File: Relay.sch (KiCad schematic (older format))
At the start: 0 parts

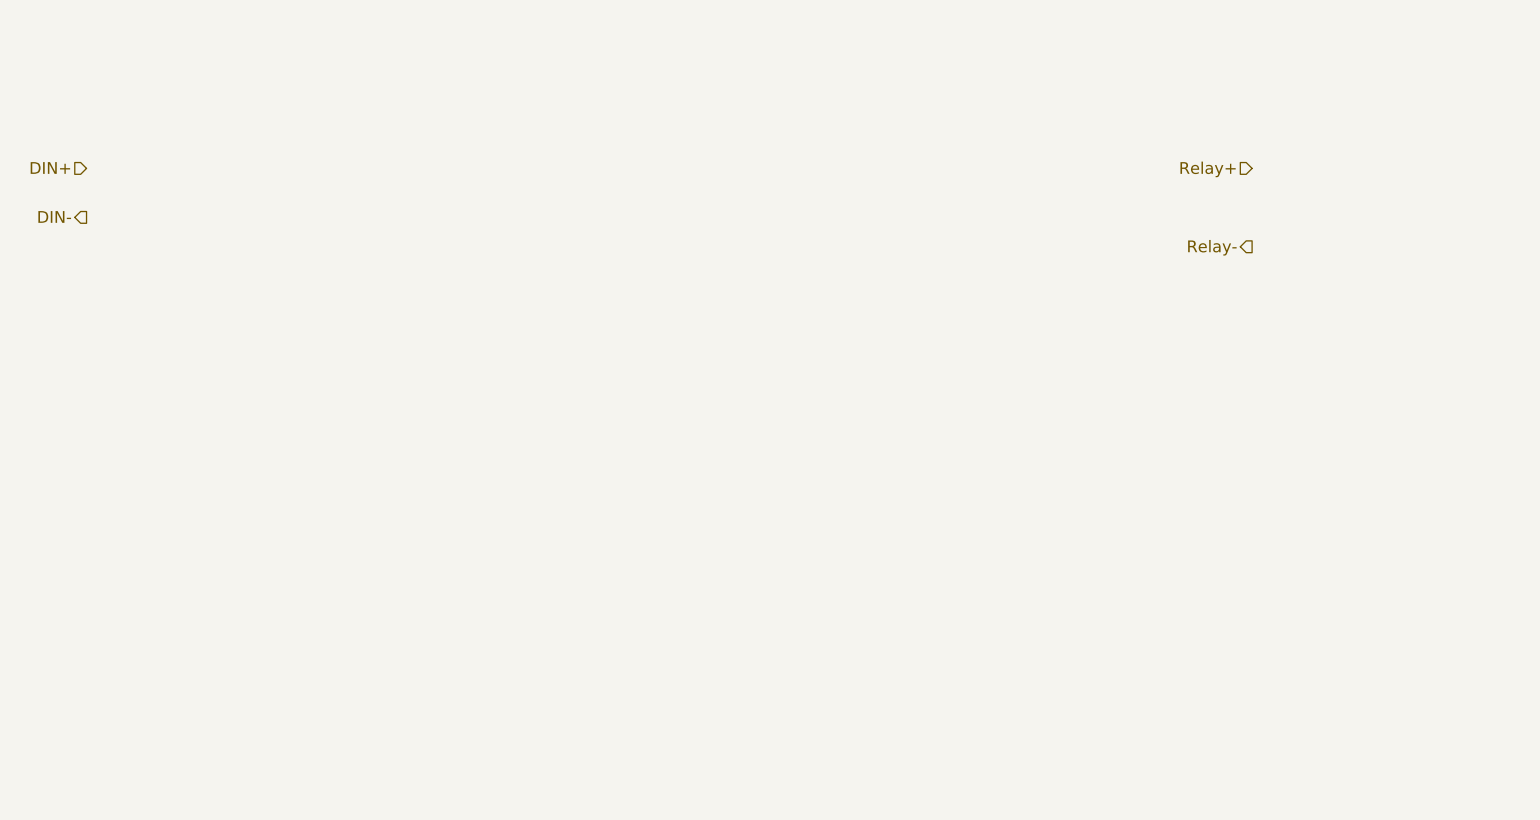
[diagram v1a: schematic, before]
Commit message: Added Relay module outline
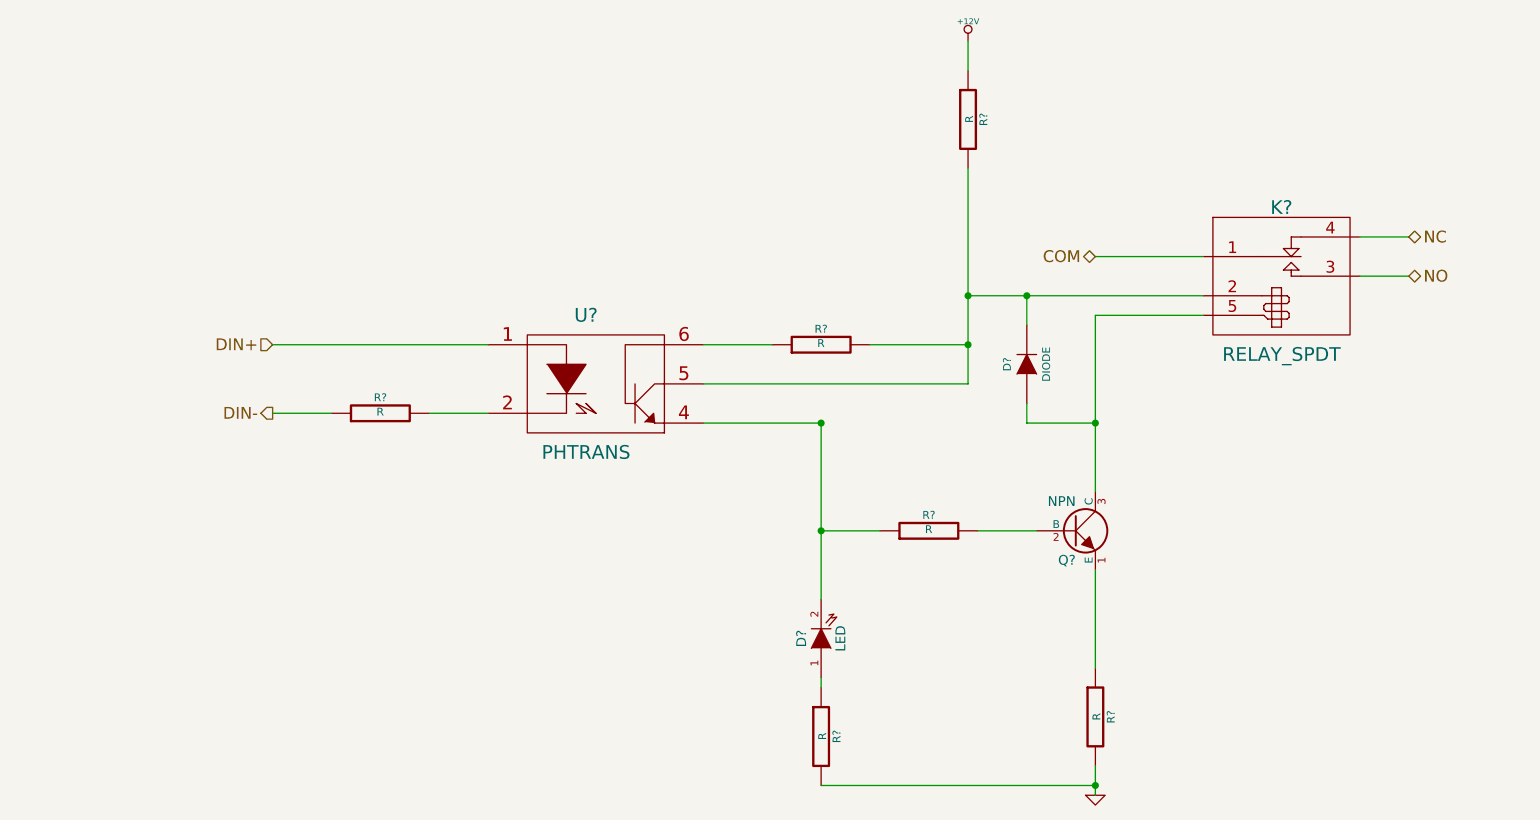
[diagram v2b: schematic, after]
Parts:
- added D?: LED, ~, symbol LED
- added D?: DIODE, ~, symbol DIODE
- added K?: RELAY_SPDT, ~, symbol RELAY_SPDT
- added Q?: NPN, ~, symbol NPN
- added R? (x6): R, ~, symbol R
- added U?: PHTRANS, ~, symbol PHTRANS
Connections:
- net DIN+: now also U?.1
- net DIN-: now also R?.1
- new net: R?.2, U?.2
- new net: D?.2 (K), R?.1, U?.4
- new net: D?.2 (K), K?.2 (Coil+), R?.2, R?.2, U?.5
- new net: R?.1, U?.6
- new net: Q?.2 (B), R?.2
- new net: Q?.1 (E), R?.1
- new net: D?.1 (A), K?.5 (Coil-), Q?.3 (C)
- new net: D?.1 (A), R?.1
- new net +12V: R?.1
- new net COM: K?.1 (C1)
- new net GND: R?.2, R?.2
- new net NC: K?.4 (R1)
- new net NO: K?.3 (T1)
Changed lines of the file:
@@
 LIBS:contrib
 LIBS:valves
+LIBS:BenchBudEE
 LIBS:BenchBudEE-cache
 EELAYER 27 0
@@
 Comment4 ""
 $EndDescr
-Text HLabel 2450 2500 0    60   Input ~ 0
+Text HLabel 3400 3400 0    60   Input ~ 0
 DIN+
-Text HLabel 2450 2750 0    60   Output ~ 0
+Text HLabel 3400 3750 0    60   Output ~ 0
 DIN-
-Text HLabel 8400 2500 0    60   Input ~ 0
-Relay+
-Text HLabel 8400 2900 0    60   Output ~ 0
-Relay-
+Text HLabel 9200 3050 2    60   BiDi ~ 0
+NO
+Text HLabel 9200 2850 2    60   BiDi ~ 0
+NC
+$Comp
+L PHTRANS U?
+U 1 1 52EFBD6E
+P 5050 3600
+F 0 "U?" H 5000 3950 70  0000 C CNN
+F 1 "PHTRANS" H 5000 3250 70  0000 C CNN
+F 2 "~" H 5050 3600 60  0000 C CNN
+F 3 "~" H 5050 3600 60  0000 C CNN
+	1    5050 3600
+	1    0    0    -1
+$EndComp
+$Comp
+L R R?
+U 1 1 52EFBD7D
+P 6750 4350
+F 0 "R?" V 6830 4350 40  0000 C CNN
+F 1 "R" V 6757 4351 40  0000 C CNN
+F 2 "~" V 6680 4350 30  0000 C CNN
+F 3 "~" H 6750 4350 30  0000 C CNN
+	1    6750 4350
+	0    -1   -1   0
+$EndComp
+$Comp
+L NPN Q?
+U 1 1 52EFBDE3
+P 7500 4350
+F 0 "Q?" H 7500 4200 50  0000 R CNN
+F 1 "NPN" H 7500 4500 50  0000 R CNN
+F 2 "~" H 7500 4350 60  0000 C CNN
+F 3 "~" H 7500 4350 60  0000 C CNN
+	1    7500 4350
+	1    0    0    -1
+$EndComp
+$Comp
+L LED D?
+U 1 1 52EFBDF2
+P 6200 4900
+F 0 "D?" H 6200 5000 50  0000 C CNN
+F 1 "LED" H 6200 4800 50  0000 C CNN
+F 2 "~" H 6200 4900 60  0000 C CNN
+F 3 "~" H 6200 4900 60  0000 C CNN
+	1    6200 4900
+	0    -1   -1   0
+$EndComp
+$Comp
+L RELAY_SPDT K?
+U 1 1 52EFC34C
+P 8550 2900
+F 0 "K?" H 8550 3100 70  0000 C CNN
+F 1 "RELAY_SPDT" H 8550 2350 70  0000 C CNN
+F 2 "~" H 8550 2900 60  0000 C CNN
+F 3 "~" H 8550 2900 60  0000 C CNN
+	1    8550 2900
+	1    0    0    -1
+$EndComp
+Text HLabel 7600 2950 0    60   BiDi ~ 0
+COM
+Wire Wire Line
+	7600 2950 8150 2950
+Wire Wire Line
+	9200 2850 8950 2850
+Wire Wire Line
+	9200 3050 8950 3050
+Wire Wire Line
+	5600 3800 6200 3800
+Wire Wire Line
+	7000 4350 7300 4350
+Wire Wire Line
+	7600 4150 7600 3250
+Wire Wire Line
+	7600 3250 8150 3250
+Wire Wire Line
+	8150 3150 6950 3150
+Wire Wire Line
+	6950 2500 6950 3600
+$Comp
+L R R?
+U 1 1 52EFC3AD
+P 7600 5300
+F 0 "R?" V 7680 5300 40  0000 C CNN
+F 1 "R" V 7607 5301 40  0000 C CNN
+F 2 "~" V 7530 5300 30  0000 C CNN
+F 3 "~" H 7600 5300 30  0000 C CNN
+	1    7600 5300
+	1    0    0    -1
+$EndComp
+Wire Wire Line
+	7600 4550 7600 5050
+$Comp
+L GND #PWR?
+U 1 1 52EFC3D1
+P 7600 5700
+F 0 "#PWR?" H 7600 5700 30  0001 C CNN
+F 1 "GND" H 7600 5630 30  0001 C CNN
+F 2 "" H 7600 5700 60  0000 C CNN
+F 3 "" H 7600 5700 60  0000 C CNN
+	1    7600 5700
+	1    0    0    -1
+$EndComp
+Wire Wire Line
+	7600 5550 7600 5700
+$Comp
+L R R?
+U 1 1 52EFC3F3
+P 6200 5400
+F 0 "R?" V 6280 5400 40  0000 C CNN
+F 1 "R" V 6207 5401 40  0000 C CNN
+F 2 "~" V 6130 5400 30  0000 C CNN
+F 3 "~" H 6200 5400 30  0000 C CNN
+	1    6200 5400
+	1    0    0    -1
+$EndComp
+Connection ~ 6200 3800
+Wire Wire Line
+	6200 5100 6200 5150
+Wire Wire Line
+	6200 5650 7600 5650
+Connection ~ 7600 5650
+$Comp
+L R R?
+U 1 1 52EFC424
+P 6950 2250
+F 0 "R?" V 7030 2250 40  0000 C CNN
+F 1 "R" V 6957 2251 40  0000 C CNN
+F 2 "~" V 6880 2250 30  0000 C CNN
+F 3 "~" H 6950 2250 30  0000 C CNN
+	1    6950 2250
+	1    0    0    -1
+$EndComp
+$Comp
+L +12V #PWR?
+U 1 1 52EFC433
+P 6950 1850
+F 0 "#PWR?" H 6950 1800 20  0001 C CNN
+F 1 "+12V" H 6950 1950 30  0000 C CNN
+F 2 "" H 6950 1850 60  0000 C CNN
+F 3 "" H 6950 1850 60  0000 C CNN
+	1    6950 1850
+	1    0    0    -1
+$EndComp
+Wire Wire Line
+	6950 1850 6950 2000
+Wire Wire Line
+	6950 3600 5600 3600
+Connection ~ 6950 3150
+$Comp
+L R R?
+U 1 1 52EFC463
+P 6200 3400
+F 0 "R?" V 6280 3400 40  0000 C CNN
+F 1 "R" V 6207 3401 40  0000 C CNN
+F 2 "~" V 6130 3400 30  0000 C CNN
+F 3 "~" H 6200 3400 30  0000 C CNN
+	1    6200 3400
+	0    -1   -1   0
+$EndComp
+Wire Wire Line
+	5600 3400 5950 3400
+Wire Wire Line
+	6450 3400 6950 3400
+Connection ~ 6950 3400
+Wire Wire Line
+	3400 3400 4500 3400
+$Comp
+L R R?
+U 1 1 52EFC4A9
+P 3950 3750
+F 0 "R?" V 4030 3750 40  0000 C CNN
+F 1 "R" V 3957 3751 40  0000 C CNN
+F 2 "~" V 3880 3750 30  0000 C CNN
+F 3 "~" H 3950 3750 30  0000 C CNN
+	1    3950 3750
+	0    -1   -1   0
+$EndComp
+Wire Wire Line
+	3400 3750 3700 3750
+Wire Wire Line
+	4200 3750 4500 3750
+$Comp
+L DIODE D?
+U 1 1 52EFC4E6
+P 7250 3500
+F 0 "D?" H 7250 3600 40  0000 C CNN
+F 1 "DIODE" H 7250 3400 40  0000 C CNN
+F 2 "~" H 7250 3500 60  0000 C CNN
+F 3 "~" H 7250 3500 60  0000 C CNN
+	1    7250 3500
+	0    -1   -1   0
+$EndComp
+Wire Wire Line
+	7250 3300 7250 3150
+Connection ~ 7250 3150
+Wire Wire Line
+	7250 3700 7250 3800
+Wire Wire Line
+	7250 3800 7600 3800
+Connection ~ 7600 3800
+Wire Wire Line
+	6200 3800 6200 4700
+Wire Wire Line
+	6500 4350 6200 4350
+Connection ~ 6200 4350
 $EndSCHEMATC

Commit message: Hooked up top level schematic
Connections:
- net COM renamed RELAY_COM
- net DIN+ renamed RELAY+
- net DIN- renamed RELAY-
- net NC renamed RELAY_NC
- net NO renamed RELAY_NO
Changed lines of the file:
@@
 $EndDescr
 Text HLabel 3400 3400 0    60   Input ~ 0
-DIN+
+RELAY+
 Text HLabel 3400 3750 0    60   Output ~ 0
-DIN-
+RELAY-
 Text HLabel 9200 3050 2    60   BiDi ~ 0
-NO
+RELAY_NO
 Text HLabel 9200 2850 2    60   BiDi ~ 0
-NC
+RELAY_NC
 $Comp
 L PHTRANS U?
@@
 $EndComp
 Text HLabel 7600 2950 0    60   BiDi ~ 0
-COM
+RELAY_COM
 Wire Wire Line
 	7600 2950 8150 2950
